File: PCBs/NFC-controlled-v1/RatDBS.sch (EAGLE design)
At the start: 20 parts

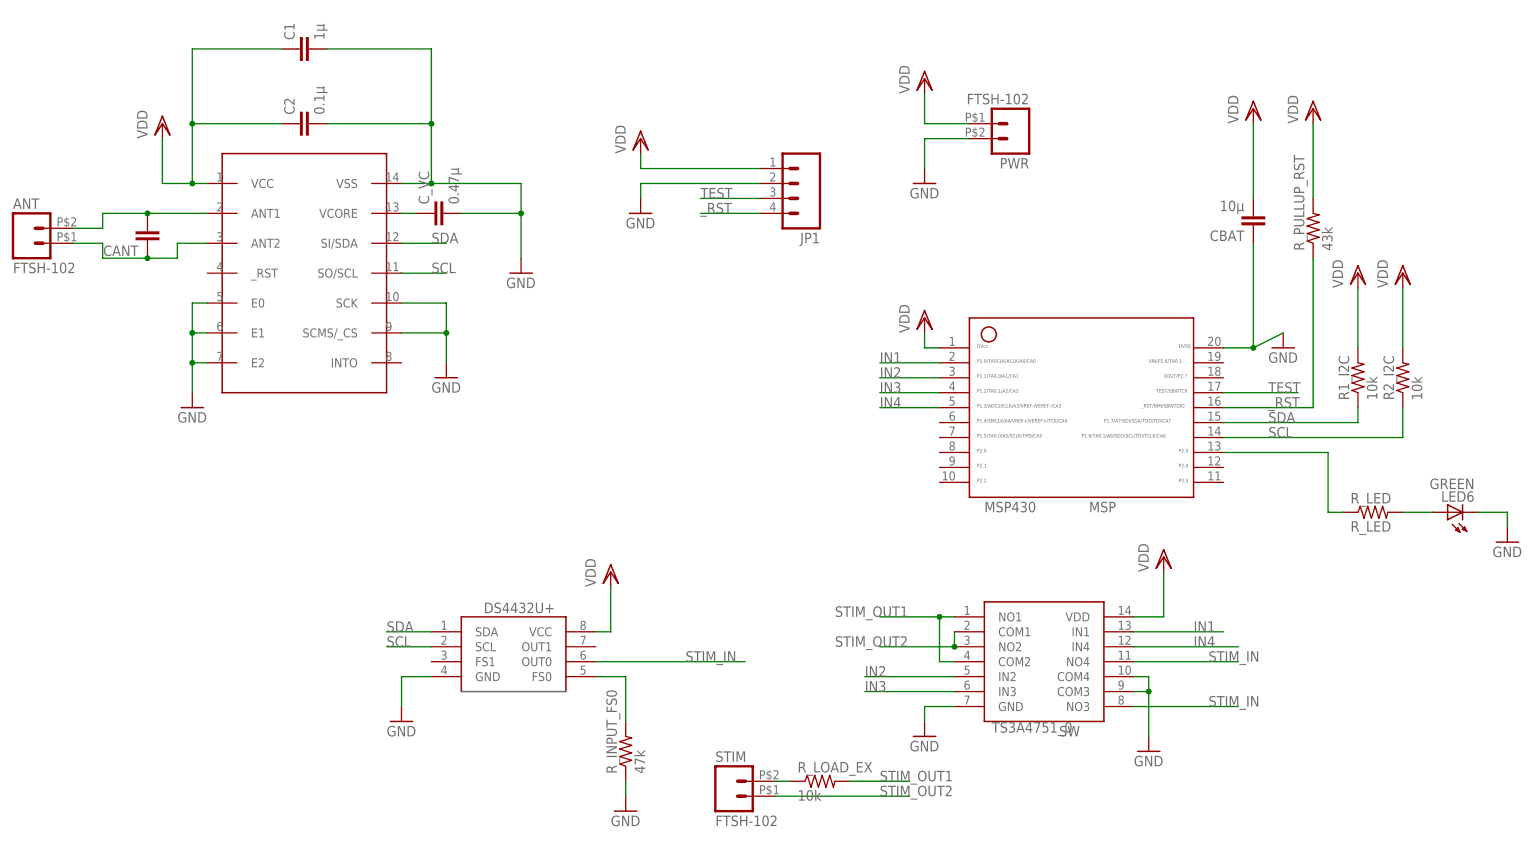
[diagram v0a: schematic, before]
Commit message: Found bug in PCB - switch matrix not wired up correctly. Fixed, and added interrupt and reset connections to MSP430
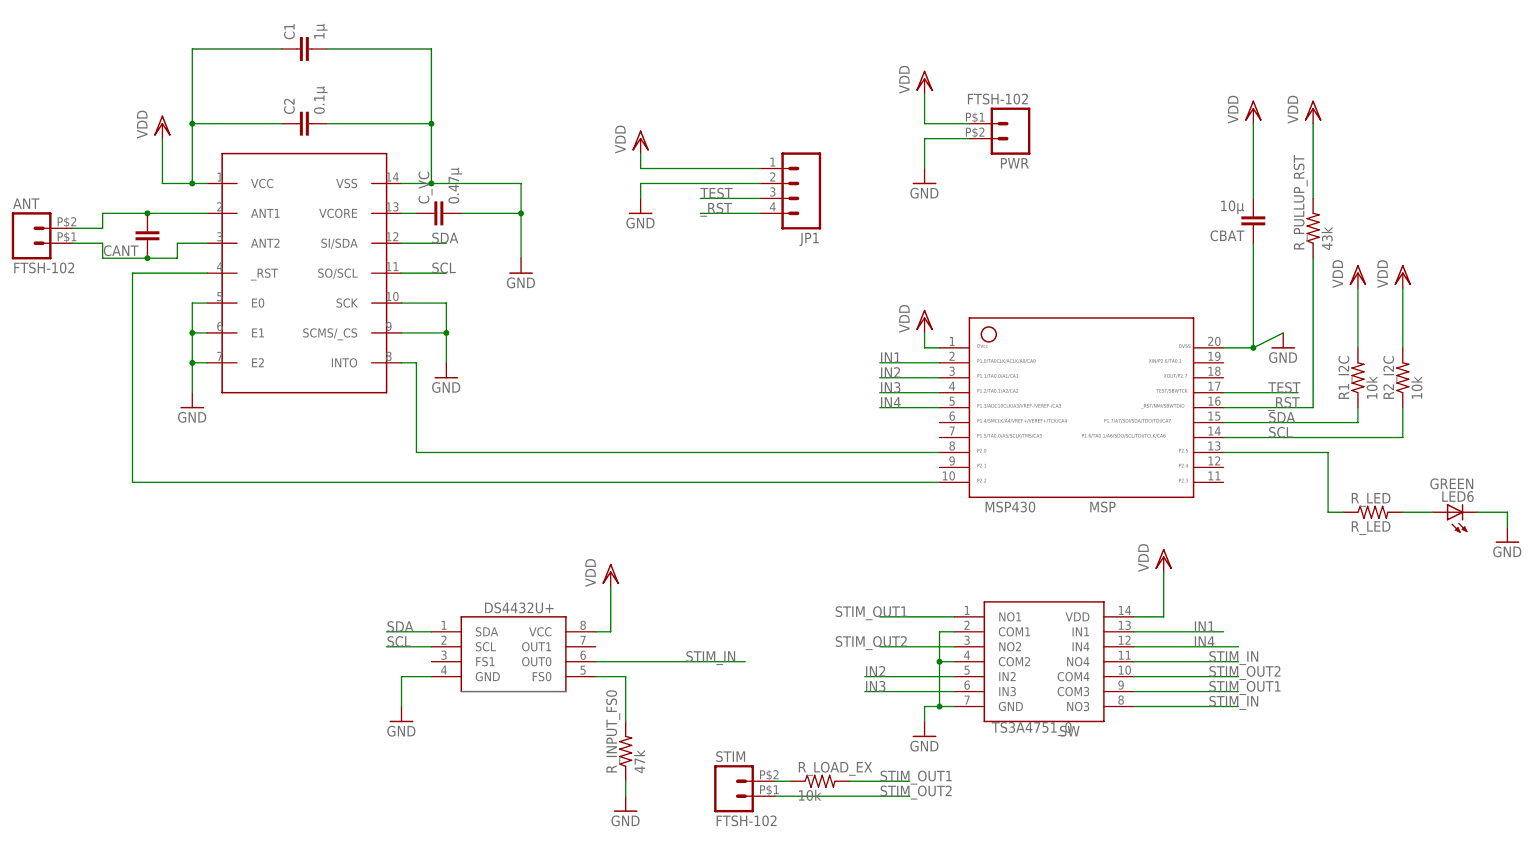
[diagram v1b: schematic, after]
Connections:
- new net N$3: MSP430.8, U$1.INTO
- new net N$7: MSP430.10, U$1._RST
- net GND: now also TS3A4751_0.COM1, TS3A4751_0.COM2; no longer TS3A4751_0.COM3, TS3A4751_0.COM4
- net STIM_OUT1: now also TS3A4751_0.COM3; no longer TS3A4751_0.COM2
- net STIM_OUT2: now also TS3A4751_0.COM4; no longer TS3A4751_0.COM1
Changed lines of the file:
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@@
 <setting verticaltext="up"/>
 </settings>
-<grid distance="0.1" unitdist="inch" unit="inch" style="lines" multiple="1" display="yes" altdistance="0.05" altunitdist="inch" altunit="inch"/>
+<grid distance="0.1" unitdist="inch" unit="inch" style="lines" multiple="1" display="no" altdistance="0.01" altunitdist="inch" altunit="inch"/>
 <layers>
 <layer number="1" name="Top" color="4" fill="1" visible="no" active="no"/>
@@
 <part name="ANT" library="Samtec50Mil" deviceset="FTSH-102" device=""/>
 <part name="CANT" library="rcl" deviceset="C-EU" device="C0603"/>
-<part name="GND11" library="supply1" deviceset="GND" device=""/>
 <part name="C1" library="rcl" deviceset="C-EU" device="C0603" value="1µ"/>
 </parts>
@@
 <instance part="ANT" gate="G$1" x="-195.58" y="101.6"/>
 <instance part="CANT" gate="G$1" x="-177.8" y="99.06" rot="R180"/>
-<instance part="GND11" gate="1" x="-7.62" y="12.7"/>
 <instance part="C1" gate="G$1" x="-152.4" y="132.08" rot="R90"/>
 </instances>
@@
 <pinref part="TS3A4751_0" gate="G$1" pin="GND"/>
 <wire x1="-45.72" y1="20.32" x2="-45.72" y2="17.78" width="0.1524" layer="91"/>
-<wire x1="-40.64" y1="20.32" x2="-45.72" y2="20.32" width="0.1524" layer="91"/>
+<wire x1="-40.64" y1="20.32" x2="-43.18" y2="20.32" width="0.1524" layer="91"/>
+<pinref part="TS3A4751_0" gate="G$1" pin="COM1"/>
+<wire x1="-43.18" y1="20.32" x2="-45.72" y2="20.32" width="0.1524" layer="91"/>
+<wire x1="-40.64" y1="33.02" x2="-43.18" y2="33.02" width="0.1524" layer="91"/>
+<pinref part="TS3A4751_0" gate="G$1" pin="COM2"/>
+<wire x1="-40.64" y1="27.94" x2="-43.18" y2="27.94" width="0.1524" layer="91"/>
+<wire x1="-43.18" y1="33.02" x2="-43.18" y2="27.94" width="0.1524" layer="91"/>
+<wire x1="-43.18" y1="27.94" x2="-43.18" y2="20.32" width="0.1524" layer="91"/>
+<junction x="-43.18" y="27.94"/>
+<junction x="-43.18" y="20.32"/>
 </segment>
 <segment>
@@
 <pinref part="GND1" gate="1" pin="GND"/>
 </segment>
-<segment>
-<pinref part="TS3A4751_0" gate="G$1" pin="COM4"/>
-<wire x1="-10.16" y1="25.4" x2="-7.62" y2="25.4" width="0.1524" layer="91"/>
-<wire x1="-7.62" y1="25.4" x2="-7.62" y2="22.86" width="0.1524" layer="91"/>
-<pinref part="TS3A4751_0" gate="G$1" pin="COM3"/>
-<wire x1="-7.62" y1="22.86" x2="-10.16" y2="22.86" width="0.1524" layer="91"/>
-<wire x1="-7.62" y1="22.86" x2="-7.62" y2="15.24" width="0.1524" layer="91"/>
-<junction x="-7.62" y="22.86"/>
-<pinref part="GND11" gate="1" pin="GND"/>
-</segment>
 </net>
 <net name="TEST" class="0">
@@
 <segment>
 <pinref part="TS3A4751_0" gate="G$1" pin="NO2"/>
-<wire x1="-40.64" y1="33.02" x2="-40.64" y2="30.48" width="0.1524" layer="91"/>
-<pinref part="TS3A4751_0" gate="G$1" pin="COM1"/>
 <wire x1="-40.64" y1="30.48" x2="-53.34" y2="30.48" width="0.1524" layer="91"/>
-<junction x="-40.64" y="30.48"/>
 <label x="-60.96" y="30.48" size="1.778" layer="95"/>
+</segment>
+<segment>
+<pinref part="TS3A4751_0" gate="G$1" pin="COM4"/>
+<wire x1="-10.16" y1="25.4" x2="7.62" y2="25.4" width="0.1524" layer="91"/>
+<label x="2.54" y="25.4" size="1.778" layer="95"/>
 </segment>
 </net>
@@
 </segment>
 <segment>
-<wire x1="-43.18" y1="35.56" x2="-40.64" y2="35.56" width="0.1524" layer="91"/>
 <pinref part="TS3A4751_0" gate="G$1" pin="NO1"/>
-<pinref part="TS3A4751_0" gate="G$1" pin="COM2"/>
-<wire x1="-40.64" y1="27.94" x2="-43.18" y2="27.94" width="0.1524" layer="91"/>
-<wire x1="-43.18" y1="27.94" x2="-43.18" y2="35.56" width="0.1524" layer="91"/>
-<wire x1="-43.18" y1="35.56" x2="-53.34" y2="35.56" width="0.1524" layer="91"/>
-<junction x="-43.18" y="35.56"/>
+<wire x1="-40.64" y1="35.56" x2="-53.34" y2="35.56" width="0.1524" layer="91"/>
 <label x="-60.96" y="35.56" size="1.778" layer="95"/>
+</segment>
+<segment>
+<pinref part="TS3A4751_0" gate="G$1" pin="COM3"/>
+<wire x1="-10.16" y1="22.86" x2="7.62" y2="22.86" width="0.1524" layer="91"/>
+<label x="2.54" y="22.86" size="1.778" layer="95"/>
 </segment>
 </net>
@@
 </segment>
 </net>
+<net name="N$3" class="0">
+<segment>
+<pinref part="U$1" gate="G$1" pin="INTO"/>
+<wire x1="-134.62" y1="78.74" x2="-132.08" y2="78.74" width="0.1524" layer="91"/>
+<wire x1="-132.08" y1="78.74" x2="-132.08" y2="63.5" width="0.1524" layer="91"/>
+<wire x1="-132.08" y1="63.5" x2="-43.18" y2="63.5" width="0.1524" layer="91"/>
+<pinref part="MSP430" gate="G$1" pin="8"/>
+</segment>
+</net>
+<net name="N$7" class="0">
+<segment>
+<pinref part="U$1" gate="G$1" pin="_RST"/>
+<wire x1="-167.64" y1="93.98" x2="-180.34" y2="93.98" width="0.1524" layer="91"/>
+<wire x1="-180.34" y1="93.98" x2="-180.34" y2="58.42" width="0.1524" layer="91"/>
+<wire x1="-180.34" y1="58.42" x2="-43.18" y2="58.42" width="0.1524" layer="91"/>
+<pinref part="MSP430" gate="G$1" pin="10"/>
+</segment>
+</net>
